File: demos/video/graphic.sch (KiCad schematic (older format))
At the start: 34 parts, among them P10 CONN_1, P11 CONN_1, P12 CONN_1, P4 CONN_2, P5 CONN_5, P9 CONN_1, U2 4C4001, U21 XC1736APD8, U23 XC4003/PQ100, U24 XC4005-PQ160, U7 AV9173, X1 10MHz

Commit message: Pcbnew: Minor fix in hotkeys. Demos: add an example to use  a local fp-lib-table and local libs, and update schematics and boards.
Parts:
- C17, C18, C19, C20, C21, C22, C23, C70, C71, C72, C73, R1, R13, R21, R26, R48: footprint (none) -> lib_smd:SM1206
- C49, C50: footprint (none) -> discret:C1
- C56: footprint (none) -> lib_smd:SM1812L
- C57, C63: footprint (none) -> lib_smd:SM1210L
- D6: footprint (none) -> discret:LEDV
- P10, P11, P9: footprint (none) -> connect:PINTST
- P12: footprint (none) -> connect:TESTPOINT
- P4: footprint (none) -> connect:SIL-2
- P5: footprint (none) -> pin_array:PIN_ARRAY_5x1
- U2: footprint (none) -> lib_smd:SO28
- U21: footprint (none) -> dip_sockets:DIP-8__300
- U23: footprint (none) -> lib_smd:PQFP100
- U24: footprint (none) -> lib_smd:PQFP160
- U7: footprint (none) -> lib_smd:SO8E
- X1: footprint (none) -> discret:HC-18UV

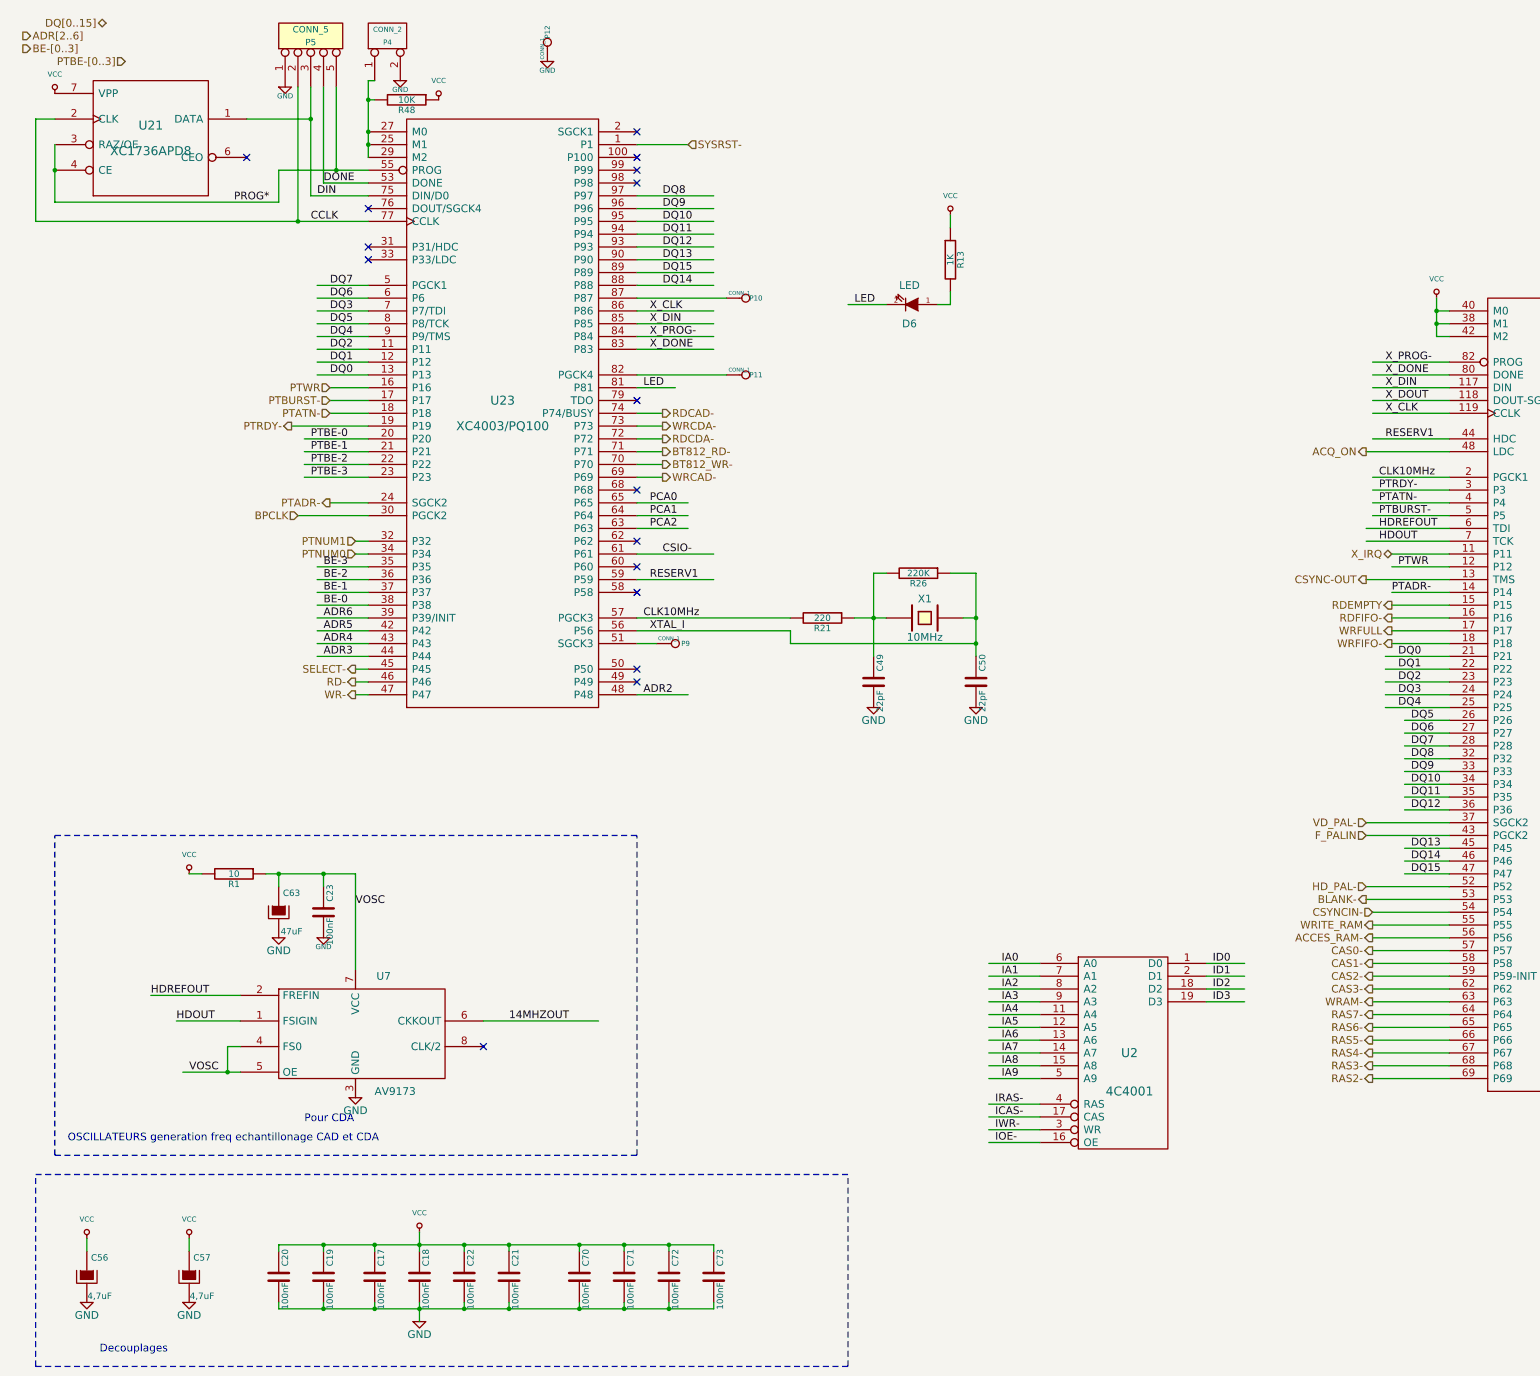
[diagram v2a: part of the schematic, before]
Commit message: demos/ schematic tidying
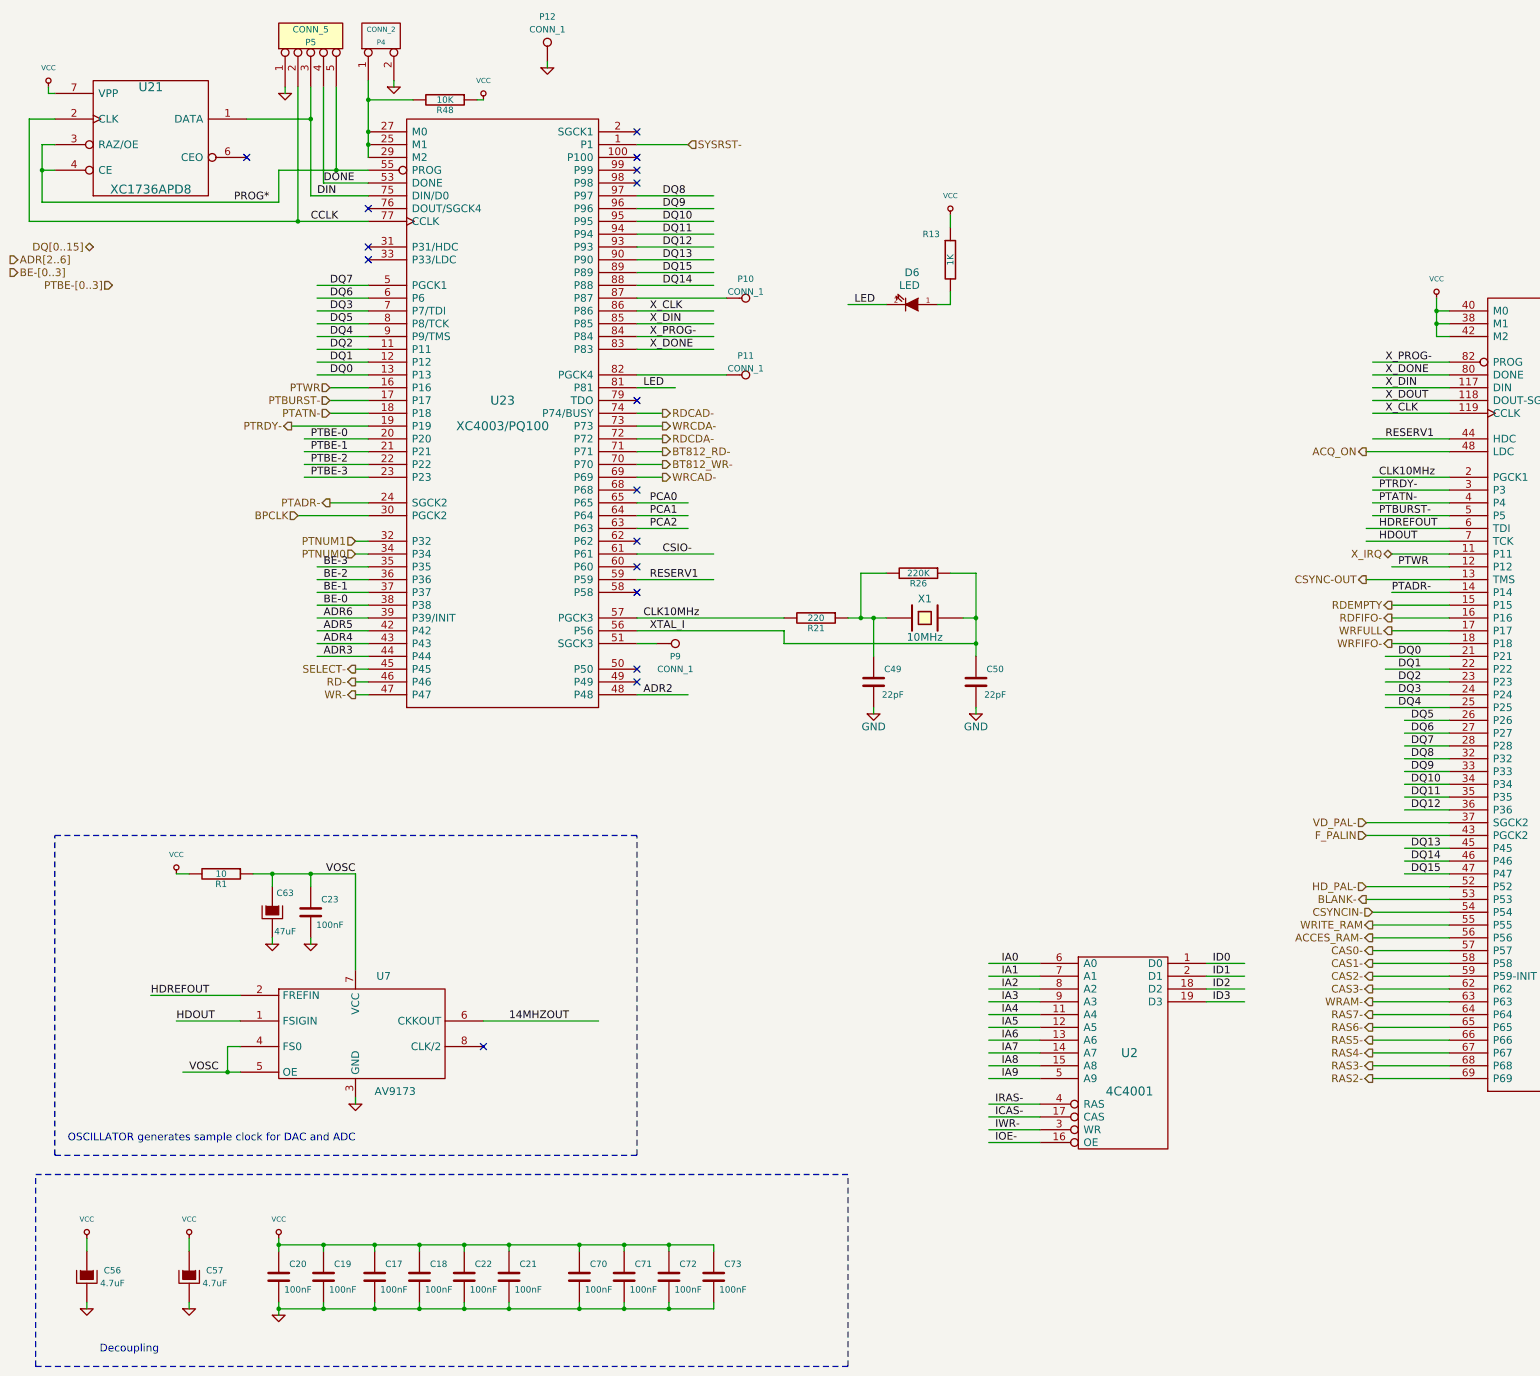
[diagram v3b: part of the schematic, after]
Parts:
- C56, C57: value 4,7uF -> 4.7uF
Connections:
- wire segments 262 -> 277
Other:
- note added: "Decoupling"
- note added: "OSCILLATOR generates sample clock for DAC and ADC"
- note removed: "Decouplages"
- note removed: "OSCILLATEURS generation freq echantillonage CAD et CDA"
- note removed: "Pour CDA"
- moved on the sheet: C23, C63, P4, R1, R21, R48

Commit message: polygons in footprint body: fix incorrect calculation of polygons with clearance or outline thickness (fix bug #1511366) Clean demos
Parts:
- C49, C50: footprint discret:C1 -> Discret:C1
- D6: footprint discret:LEDV -> Discret:LEDV
- P10, P11, P9: footprint connect:PINTST -> Connect:PINTST
- P12: footprint connect:TESTPOINT -> Connect:TESTPOINT
- P4: footprint connect:SIL-2 -> Connect:SIL-2
- X1: footprint discret:HC-18UV -> Discret:HC-18UV
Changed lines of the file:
@@
 EESchema Schematic File Version 2
+LIBS:video_schlib
 LIBS:power
-LIBS:device
-LIBS:transistors
-LIBS:conn
-LIBS:linear
-LIBS:regul
-LIBS:74xx
-LIBS:cmos4000
-LIBS:adc-dac
-LIBS:memory
-LIBS:xilinx
-LIBS:special
-LIBS:analog_switches
-LIBS:motorola
-LIBS:intel
-LIBS:audio
-LIBS:interface
-LIBS:philips
-LIBS:cypress
-LIBS:siliconi
 LIBS:video-cache
 EELAYER 25 0
@@
 F 0 "P12" V 5050 800 50  0000 C CNN
 F 1 "CONN_1" V 4950 800 50  0000 C CNN
-F 2 "connect:TESTPOINT" H 4850 800 60  0001 C CNN
+F 2 "Connect:TESTPOINT" H 4850 800 60  0001 C CNN
 F 3 "" H 4850 800 60  0001 C CNN
 	1    4850 800
@@
 F 0 "P9" H 5850 5400 50  0000 C CNN
 F 1 "CONN_1" H 5850 5300 50  0000 C CNN
-F 2 "connect:PINTST" H 5850 5500 60  0001 C CNN
+F 2 "Connect:PINTST" H 5850 5500 60  0001 C CNN
 F 3 "" H 5850 5500 60  0001 C CNN
 	1    5850 5500
@@
 F 0 "P11" H 6400 3550 50  0000 C CNN
 F 1 "CONN_1" H 6400 3450 50  0000 C CNN
-F 2 "connect:PINTST" H 6400 3400 60  0001 C CNN
+F 2 "Connect:PINTST" H 6400 3400 60  0001 C CNN
 F 3 "" H 6400 3400 60  0001 C CNN
 	1    6400 3400
@@
 F 0 "P10" H 6400 2950 50  0000 C CNN
 F 1 "CONN_1" H 6400 2850 50  0000 C CNN
-F 2 "connect:PINTST" H 6400 2800 60  0001 C CNN
+F 2 "Connect:PINTST" H 6400 2800 60  0001 C CNN
 F 3 "" H 6400 2800 60  0001 C CNN
 	1    6400 2800
@@
 F 0 "P4" V 3500 750 40  0000 C CNN
 F 1 "CONN_2" V 3600 750 40  0000 C CNN
-F 2 "connect:SIL-2" H 3550 750 60  0001 C CNN
+F 2 "Connect:SIL-2" H 3550 750 60  0001 C CNN
 F 3 "" H 3550 750 60  0001 C CNN
 	1    3550 750
@@
 F 0 "D6" H 7700 2600 60  0000 C CNN
 F 1 "LED" H 7720 2700 60  0000 C CNN
-F 2 "discret:LEDV" H 7700 2850 60  0001 C CNN
+F 2 "Discret:LEDV" H 7700 2850 60  0001 C CNN
 F 3 "" H 7700 2850 60  0001 C CNN
 	1    7700 2850
@@
 F 0 "C49" H 7550 5900 50  0000 C CNN
 F 1 "22pF" H 7550 5700 50  0000 C CNN
-F 2 "discret:C1" H 7400 5800 60  0001 C CNN
+F 2 "Discret:C1" H 7400 5800 60  0001 C CNN
 F 3 "" H 7400 5800 60  0001 C CNN
 	1    7400 5800
@@
 F 0 "C50" H 8350 5900 50  0000 C CNN
 F 1 "22pF" H 8350 5700 50  0000 C CNN
-F 2 "discret:C1" H 8200 5800 60  0001 C CNN
+F 2 "Discret:C1" H 8200 5800 60  0001 C CNN
 F 3 "" H 8200 5800 60  0001 C CNN
 	1    8200 5800
@@
 F 0 "X1" H 7800 5450 60  0000 C CNN
 F 1 "10MHz" H 7800 5150 60  0000 C CNN
-F 2 "discret:HC-18UV" H 7800 5300 60  0001 C CNN
+F 2 "Discret:HC-18UV" H 7800 5300 60  0001 C CNN
 F 3 "" H 7800 5300 60  0001 C CNN
 	1    7800 5300

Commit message: merge from production git:e53c3af 21.04.2017
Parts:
- P10, P11, P9: footprint Connect:PINTST -> Connectors:PINTST
- P12: footprint Connect:TESTPOINT -> Connectors:TESTPOINT
- P4: footprint Connect:SIL-2 -> Connectors:SIL-2
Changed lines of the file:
@@
 LIBS:power
 LIBS:video-cache
-EELAYER 25 0
+EELAYER 26 0
 EELAYER END
 $Descr A3 16535 11693
@@
 F 0 "P12" V 5050 800 50  0000 C CNN
 F 1 "CONN_1" V 4950 800 50  0000 C CNN
-F 2 "Connect:TESTPOINT" H 4850 800 60  0001 C CNN
+F 2 "Connectors:TESTPOINT" H 4850 800 60  0001 C CNN
 F 3 "" H 4850 800 60  0001 C CNN
 	1    4850 800
@@
 F 0 "P9" H 5850 5400 50  0000 C CNN
 F 1 "CONN_1" H 5850 5300 50  0000 C CNN
-F 2 "Connect:PINTST" H 5850 5500 60  0001 C CNN
+F 2 "Connectors:PINTST" H 5850 5500 60  0001 C CNN
 F 3 "" H 5850 5500 60  0001 C CNN
 	1    5850 5500
@@
 F 0 "P11" H 6400 3550 50  0000 C CNN
 F 1 "CONN_1" H 6400 3450 50  0000 C CNN
-F 2 "Connect:PINTST" H 6400 3400 60  0001 C CNN
+F 2 "Connectors:PINTST" H 6400 3400 60  0001 C CNN
 F 3 "" H 6400 3400 60  0001 C CNN
 	1    6400 3400
@@
 F 0 "P10" H 6400 2950 50  0000 C CNN
 F 1 "CONN_1" H 6400 2850 50  0000 C CNN
-F 2 "Connect:PINTST" H 6400 2800 60  0001 C CNN
+F 2 "Connectors:PINTST" H 6400 2800 60  0001 C CNN
 F 3 "" H 6400 2800 60  0001 C CNN
 	1    6400 2800
@@
 F 0 "P4" V 3500 750 40  0000 C CNN
 F 1 "CONN_2" V 3600 750 40  0000 C CNN
-F 2 "Connect:SIL-2" H 3550 750 60  0001 C CNN
+F 2 "Connectors:SIL-2" H 3550 750 60  0001 C CNN
 F 3 "" H 3550 750 60  0001 C CNN
 	1    3550 750
